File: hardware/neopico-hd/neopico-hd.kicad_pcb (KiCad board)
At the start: 2 copper layers, 70 x 73.1 mm, 28 parts, among them J1 HDMI_A, J2 Conn_02x05_Top_Bottom, J4 Audio, J5 AUX, J6 Conn_01x02_Pin, SW1 MENU, SW2 BACK, U1 A_BUFF, U2 V_BUFF, U3 RG_LVS, U4 GB_LVS, U5 AV_LVS

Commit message: Fix typo
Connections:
- net MVS_PCKL renamed MVS_PCLK
- net PCKL renamed PCLK
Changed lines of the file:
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@@
 	(net 11 "B4")
 	(net 12 "G4")
-	(net 13 "PCKL")
+	(net 13 "PCLK")
 	(net 14 "D2+")
 	(net 15 "unconnected-(A1-GPIO9-Pad15)")
@@
 	(net 55 "MVS_BCK")
 	(net 56 "unconnected-(U1-2Y-Pad4)")
-	(net 57 "MVS_PCKL")
+	(net 57 "MVS_PCLK")
 	(net 58 "MVS_CSYNC")
 	(net 59 "MVS_G2")
@@
 			(layers "*.Cu" "*.Mask")
 			(remove_unused_layers no)
-			(net 13 "PCKL")
+			(net 13 "PCLK")
 			(pinfunction "GPIO28")
 			(pintype "bidirectional")
@@
 			(layers "*.Cu" "*.Mask")
 			(remove_unused_layers no)
-			(net 57 "MVS_PCKL")
+			(net 57 "MVS_PCLK")
 			(pinfunction "Pin_19")
 			(pintype "passive")
@@
 			(layers "F.Cu" "F.Mask" "F.Paste")
 			(roundrect_rratio 0.25)
-			(net 57 "MVS_PCKL")
+			(net 57 "MVS_PCLK")
 			(pinfunction "2A")
 			(pintype "input")
@@
 			(layers "F.Cu" "F.Mask" "F.Paste")
 			(roundrect_rratio 0.25)
-			(net 13 "PCKL")
+			(net 13 "PCLK")
 			(pinfunction "2Y")
 			(pintype "output")

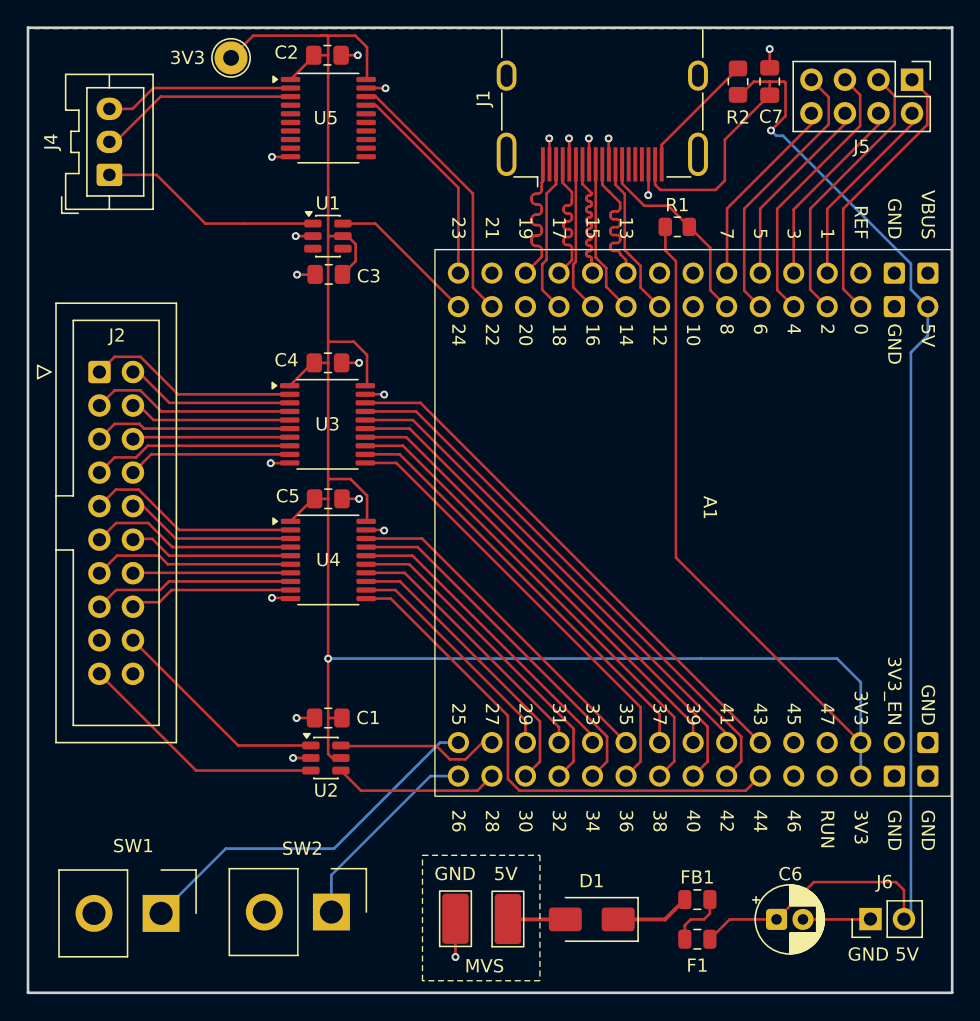
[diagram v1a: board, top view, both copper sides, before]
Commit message: Hardware - add HDMI termination resistors and more
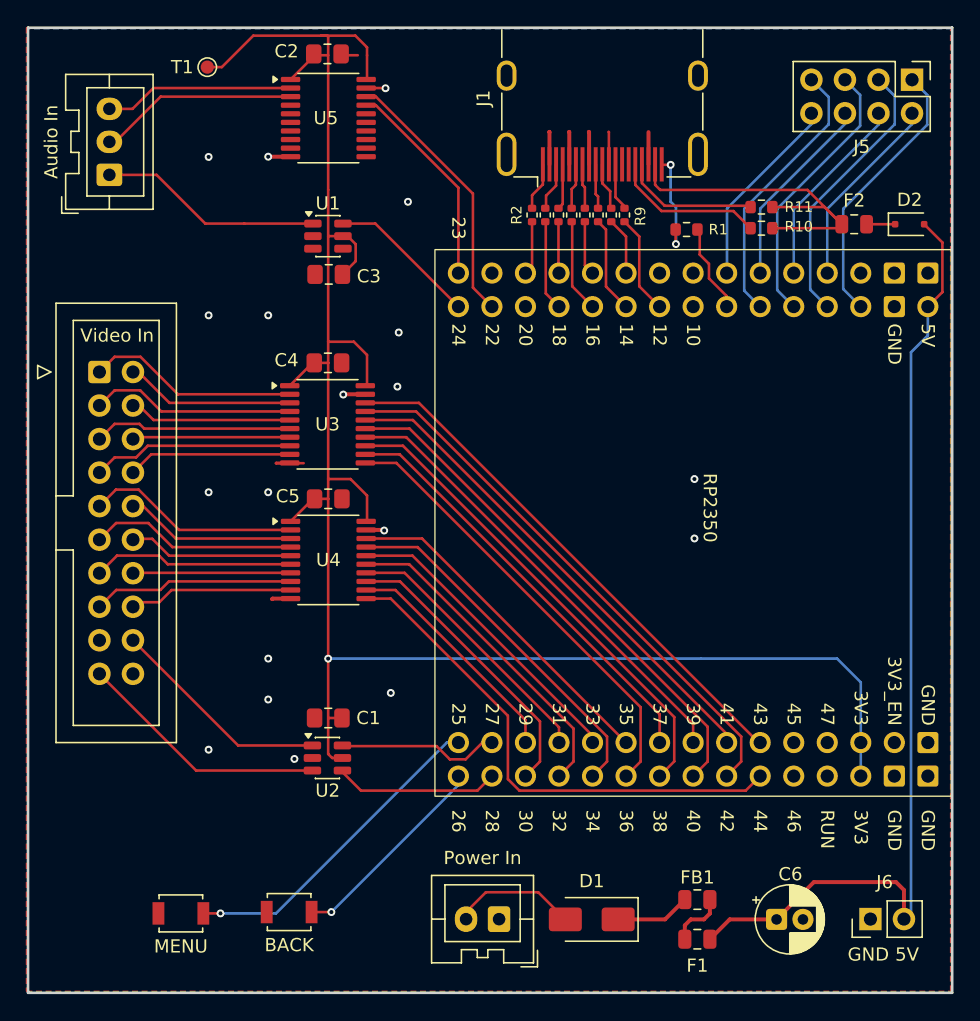
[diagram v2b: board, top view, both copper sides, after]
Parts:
- removed 3V3: TestPoint_THTPad_D2.5mm_Drill1.2mm, TestPoint:TestPoint_THTPad_D2.5mm_Drill1.2mm
- removed C7: 0.1u, Capacitor_SMD:C_0805_2012Metric_Pad1.18x1.45mm_HandSolder
- removed the R1 at (164.7, 50.1)
- removed REF** (x2): TestPoint_Keystone_5019_Miniature, TestPoint:TestPoint_Keystone_5019_Miniature
- added D2: BAT54J, Diode_SMD:D_SOD-323F, F.Cu at (182.3, 49.9)
- added F2: MF-PSMF020X-2, Fuse:Fuse_0805_2012Metric, F.Cu at (178.1, 49.9)
- added Power In: JST_XA_B02B-XASK-1_1x02_P2.50mm_Vertical, Connector_JST:JST_XA_B02B-XASK-1_1x02_P2.50mm_Vertical, F.Cu at (151.2, 102.5)
- added R10: 2.2k, Resistor_SMD:R_0603_1608Metric, F.Cu at (171.1, 50.2)
- added R11: 2.2k, Resistor_SMD:R_0603_1608Metric, F.Cu at (171.1, 48.6)
- added R2: 270, Resistor_SMD:R_0402_1005Metric, F.Cu at (153.7, 49.2)
- added R3: 270, Resistor_SMD:R_0402_1005Metric, F.Cu at (154.7, 49.2)
- added R4: 270, Resistor_SMD:R_0402_1005Metric, F.Cu at (155.7, 49.2)
- added R5: 270, Resistor_SMD:R_0402_1005Metric, F.Cu at (156.7, 49.2)
- added R6: 270, Resistor_SMD:R_0402_1005Metric, F.Cu at (157.7, 49.2)
- added R7: 270, Resistor_SMD:R_0402_1005Metric, F.Cu at (158.7, 49.2)
- added R8: 270, Resistor_SMD:R_0402_1005Metric, F.Cu at (159.7, 49.2)
- added R9: 270, Resistor_SMD:R_0402_1005Metric, F.Cu at (160.7, 49.2)
- added T1: TestPoint_Pad_D1.0mm, TestPoint:TestPoint_Pad_D1.0mm, F.Cu at (129.1, 38.0)
- Audio In: renamed from J4
- BACK: renamed from SW2; footprint Connector_Samtec_HPM_THT:Samtec_HPM-02-01-x-S_Straight_1x02_Pitch5.08mm -> Button_Switch_SMD:SW_SPST_B3U-1000P
- MENU: renamed from SW1; footprint Connector_Samtec_HPM_THT:Samtec_HPM-02-01-x-S_Straight_1x02_Pitch5.08mm -> Button_Switch_SMD:SW_SPST_B3U-1000P
- R1: renamed from R2; footprint Resistor_SMD:R_0805_2012Metric_Pad1.20x1.40mm_HandSolder -> Resistor_SMD:R_0603_1608Metric
- Video In: renamed from J2
- moved R1 11.9 mm to (165.4, 50.3), turned to 180 degrees
- moved BACK 3.20 mm to (135.3, 102.0), turned to 180 degrees
- moved MENU 1.50 mm to (127.1, 102.1), turned to 180 degrees
- moved U2 0.12 mm to (138.2, 90.3)
- moved C2 0.10 mm to (138.2, 37.0)
- renumbered A1 to RP2350
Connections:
- J1 pad 1: D2+ -> Net-(J1-D2+)
- J1 pad 10: CLK+ -> Net-(J1-CK+)
- J1 pad 12: CLK- -> Net-(J1-CK-)
- J1 pad 13: CEC_PICO -> unconnected-(J1-CEC-Pad13)
- J1 pad 15: unconnected-(J1-SCL-Pad15) -> Net-(J1-SCL)
- J1 pad 16: unconnected-(J1-SDA-Pad16) -> Net-(J1-SDA)
- J1 pad 18: +5V -> Net-(J1-+5V)
- J1 pad 3: D2- -> Net-(J1-D2-)
- J1 pad 4: D1+ -> Net-(J1-D1+)
- J1 pad 6: D1- -> Net-(J1-D1-)
- J1 pad 7: D0+ -> Net-(J1-D0+)
- J1 pad 9: D0- -> Net-(J1-D0-)
- R1 pad 1: +5V -> HPD
- RP2350 pad 14: CEC_PICO -> HPD
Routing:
- net +3V3: track 191.3 -> 148.3 mm
- net +5V: track 109.0 -> 73.3 mm, vias 1 -> 0
- net Net-(J1-+5V): track 0.00 -> 28.1 mm
- net CEC_PICO: track 15.1 -> 0.00 mm
- net GND: track 38.3 -> 25.3 mm, vias 20 -> 19
- net Net-(J1-SCL): track 0.00 -> 11.6 mm
- net Net-(J1-SDA): track 0.00 -> 10.4 mm
- net CLK+: track 12.1 -> 4.35 mm
- net D2+: track 11.6 -> 4.10 mm
- net D1+: track 11.4 -> 3.91 mm
- net D0+: track 11.6 -> 4.13 mm
- net HPD: track 0.00 -> 6.76 mm
- net +5V MVS: track 4.36 -> 9.53 mm
- net D2-: track 11.7 -> 6.85 mm
- net CLK-: track 12.2 -> 7.53 mm
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- added copper zone on F.Cu, net GND
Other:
- board text added: "R9"
- board text removed: "MVS"
